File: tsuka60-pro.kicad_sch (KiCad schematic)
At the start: 168 parts, among them J1 USB_C_Receptacle_USB2.0, J2 Conn_01x04_MountingPin, SW1 SW_Reset, U1 ATmega32U4-M, U2 SRV05-4, Y1 16MHz

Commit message: Transferring updates from the Katana60 Pro
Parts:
- J2: footprint Connector_JST:JST_SH_SM04B-SRSS-TB_1x04-1MP_P1.00mm_Horizontal -> Connector_JST:JST_ACH_BM04B-ACHSS-A-GAN-ETF_1x04-1MP_P1.20mm_Vertical
- renumbered MX37-2 to MX37_2, MX39-2 to MX39_2
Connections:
- net 38-2 renamed 37_2
- net 39-2 renamed 39_2
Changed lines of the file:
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@@
     )
   )
-  (global_label "39-2" (shape input) (at 153.67 133.35 180) (fields_autoplaced)
+  (global_label "39_2" (shape input) (at 153.67 133.35 180) (fields_autoplaced)
     (effects (font (size 1.27 1.27)) (justify right))
-    (property "Intersheet References" "${INTERSHEET_REFS}" (id 0) (at 146.0559 133.2706 0)
+    (property "Intersheet References" "${INTERSHEET_REFS}" (id 0) (at 146.6607 133.2706 0)
       (effects (font (size 1.27 1.27)) (justify right) hide)
     )
@@
     )
   )
-  (global_label "38-2" (shape input) (at 128.27 260.35 180) (fields_autoplaced)
+  (global_label "37_2" (shape input) (at 128.27 260.35 180) (fields_autoplaced)
     (effects (font (size 1.27 1.27)) (justify right))
-    (property "Intersheet References" "${INTERSHEET_REFS}" (id 0) (at 120.6559 260.2706 0)
+    (property "Intersheet References" "${INTERSHEET_REFS}" (id 0) (at 121.2607 260.2706 0)
       (effects (font (size 1.27 1.27)) (justify right) hide)
     )
@@
     )
   )
-  (global_label "39-2" (shape input) (at 153.67 260.35 180) (fields_autoplaced)
+  (global_label "39_2" (shape input) (at 153.67 260.35 180) (fields_autoplaced)
     (effects (font (size 1.27 1.27)) (justify right))
-    (property "Intersheet References" "${INTERSHEET_REFS}" (id 0) (at 146.0559 260.2706 0)
+    (property "Intersheet References" "${INTERSHEET_REFS}" (id 0) (at 146.6607 260.2706 0)
       (effects (font (size 1.27 1.27)) (justify right) hide)
     )
@@
     )
   )
-  (global_label "38-2" (shape input) (at 128.27 133.35 180) (fields_autoplaced)
+  (global_label "37_2" (shape input) (at 128.27 133.35 180) (fields_autoplaced)
     (effects (font (size 1.27 1.27)) (justify right))
-    (property "Intersheet References" "${INTERSHEET_REFS}" (id 0) (at 120.6559 133.2706 0)
+    (property "Intersheet References" "${INTERSHEET_REFS}" (id 0) (at 121.2607 133.2706 0)
       (effects (font (size 1.27 1.27)) (justify right) hide)
     )
@@
       (effects (font (size 1.27 1.27)) (justify left))
     )
-    (property "Footprint" "Connector_JST:JST_SH_SM04B-SRSS-TB_1x04-1MP_P1.00mm_Horizontal" (id 2) (at 355.6 201.93 0)
+    (property "Footprint" "Connector_JST:JST_ACH_BM04B-ACHSS-A-GAN-ETF_1x04-1MP_P1.20mm_Vertical" (id 2) (at 355.6 201.93 0)
       (effects (font (size 1.27 1.27)) hide)
     )
@@
   (symbol (lib_id "MX_Alps_Hybrid:MX-NoLED") (at 154.94 256.54 0) (unit 1)
     (in_bom yes) (on_board yes) (fields_autoplaced)
-    (property "Reference" "MX39-2" (id 0) (at 155.8256 250.19 0)
+    (property "Reference" "MX39_2" (id 0) (at 155.8256 250.19 0)
       (effects (font (size 1.524 1.524)))
     )
@@
   (symbol (lib_id "MX_Alps_Hybrid:MX-NoLED") (at 129.54 256.54 0) (unit 1)
     (in_bom yes) (on_board yes) (fields_autoplaced)
-    (property "Reference" "MX37-2" (id 0) (at 130.4256 250.19 0)
+    (property "Reference" "MX37_2" (id 0) (at 130.4256 250.19 0)
       (effects (font (size 1.524 1.524)))
     )
@@
     )
     (path "/08e6d373-2bf3-4f1e-87e0-beb65fb65c5f"
-      (reference "J2") (unit 1) (value "Conn_01x04_MountingPin") (footprint "Connector_JST:JST_SH_SM04B-SRSS-TB_1x04-1MP_P1.00mm_Horizontal")
+      (reference "J2") (unit 1) (value "Conn_01x04_MountingPin") (footprint "Connector_JST:JST_ACH_BM04B-ACHSS-A-GAN-ETF_1x04-1MP_P1.20mm_Vertical")
     )
     (path "/bb3a180f-cdbc-49d0-97a9-6846eb214c84"
@@
     )
     (path "/f5c00a1c-6009-46f7-bb45-59e86d627cba"
-      (reference "MX37-2") (unit 1) (value "MX-NoLED") (footprint "marbastlib-mx:SW_MX_HS_1.25u")
+      (reference "MX37_2") (unit 1) (value "MX-NoLED") (footprint "marbastlib-mx:SW_MX_HS_1.25u")
     )
     (path "/75294b3a-bcf4-4dee-b1b0-009fd10bd357"
@@
     )
     (path "/a8b3e0bc-cfe9-4e81-954e-c1b4323435ec"
-      (reference "MX39-2") (unit 1) (value "MX-NoLED") (footprint "marbastlib-mx:SW_MX_HS_1.25u")
+      (reference "MX39_2") (unit 1) (value "MX-NoLED") (footprint "marbastlib-mx:SW_MX_HS_1.25u")
     )
     (path "/f1689421-be27-441f-a091-cda9d302f953"

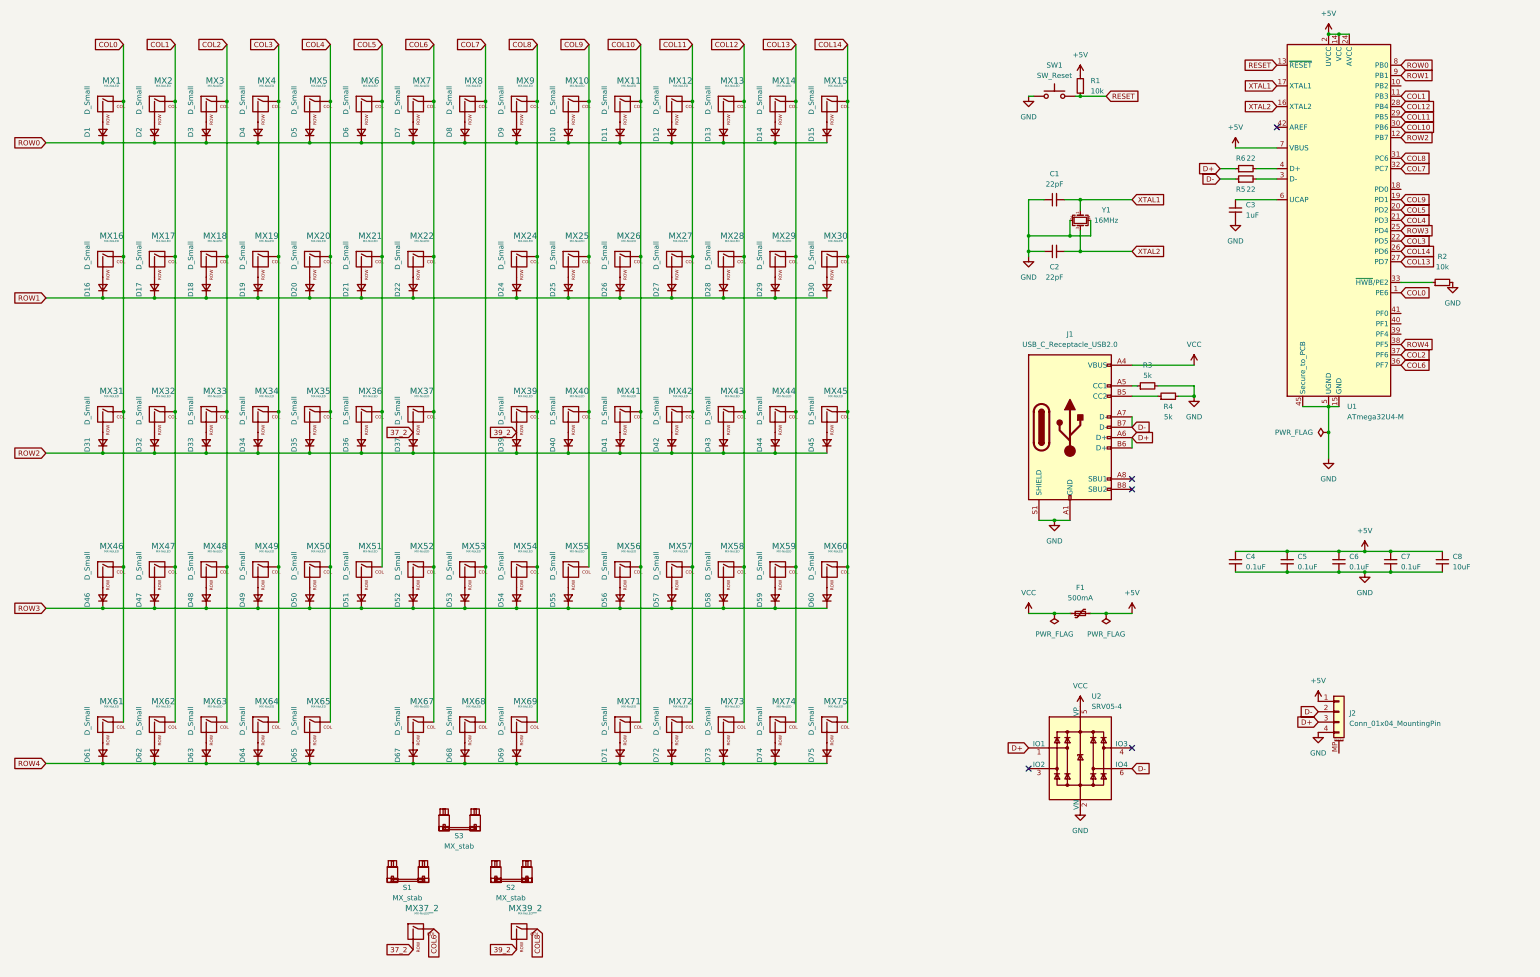
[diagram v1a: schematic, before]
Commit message: Update the schematic, footprints and layout
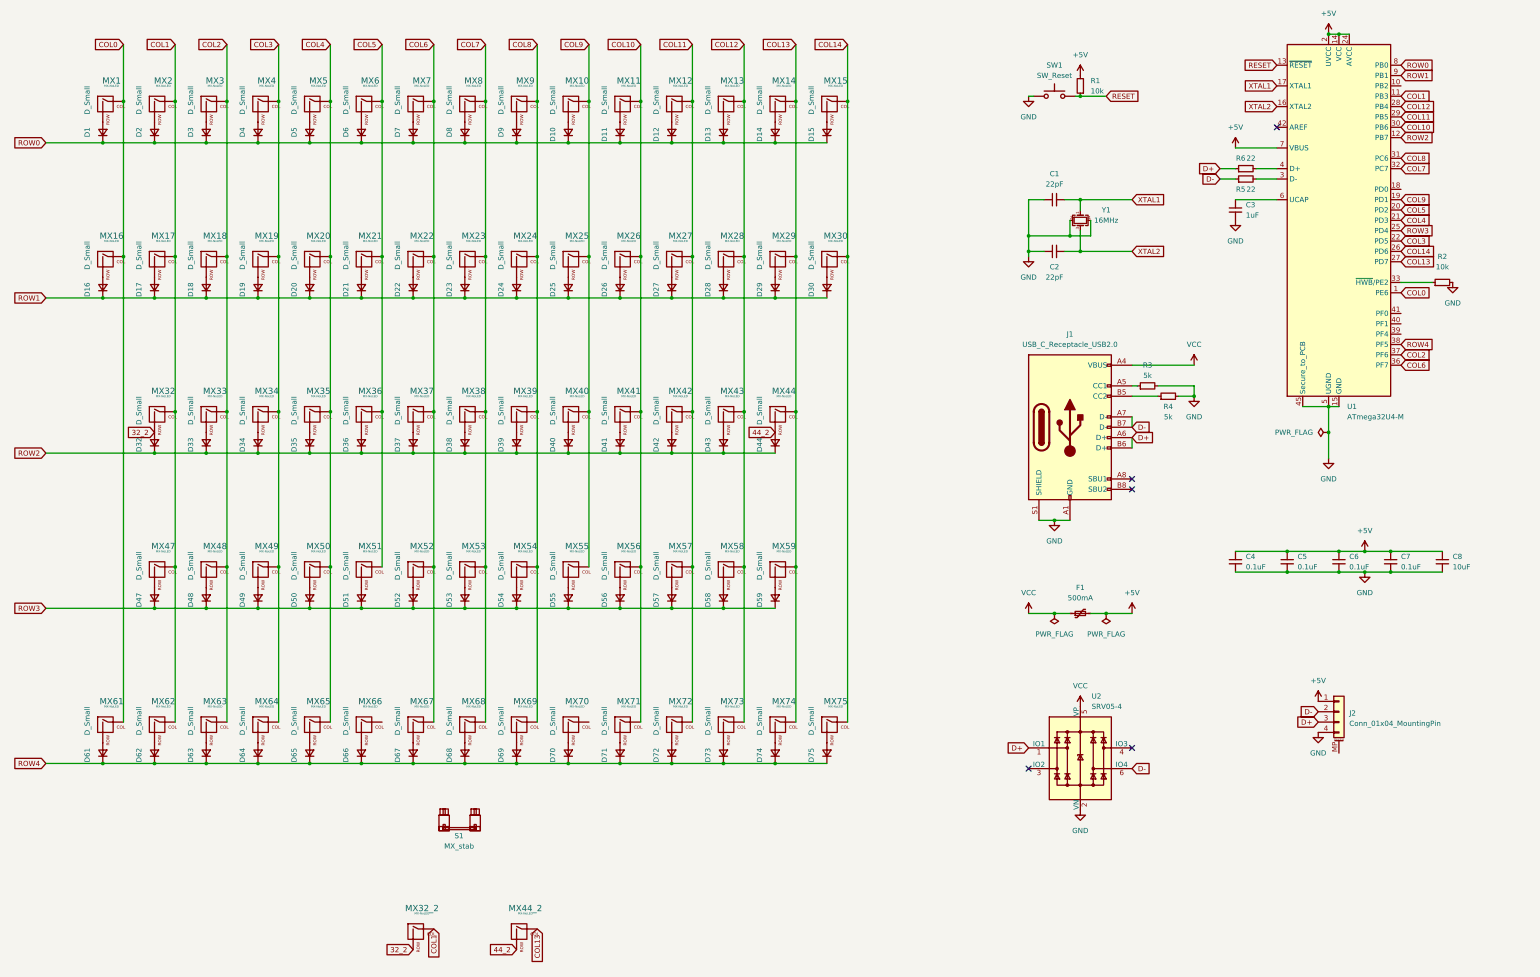
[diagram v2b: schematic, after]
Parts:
- removed D31, D45, D46, D60: D_Small, Diode_SMD:D_SOD-123, symbol Device:D_Small
- removed MX31, MX45: MX-NoLED, marbastlib-mx:SW_MX_HS_1.25u, symbol MX_Alps_Hybrid:MX-NoLED
- removed MX46, MX60: MX-NoLED, marbastlib-mx:SW_MX_HS_1u, symbol MX_Alps_Hybrid:MX-NoLED
- removed S1, S2: MX_stab, marbastlib-mx:STAB_MX_2u, symbol marbastlib-mx:MX_stab
- added D23, D38, D66, D70: D_Small, Diode_SMD:D_SOD-123, symbol Device:D_Small
- added MX23: MX-NoLED, marbastlib-mx:SW_MX_HS_1u, symbol MX_Alps_Hybrid:MX-NoLED
- added MX38: MX-NoLED, marbastlib-mx:SW_MX_HS_1.5u, symbol MX_Alps_Hybrid:MX-NoLED
- added MX66, MX70: MX-NoLED, marbastlib-mx:SW_MX_HS_1.25u, symbol MX_Alps_Hybrid:MX-NoLED
- MX16, MX30: footprint marbastlib-mx:SW_MX_HS_1.5u -> marbastlib-mx:SW_MX_HS_1u
- MX32, MX44: footprint marbastlib-mx:SW_MX_HS_1u -> marbastlib-mx:SW_MX_HS_1.75u
- MX32_2: renamed from MX37_2; footprint marbastlib-mx:SW_MX_HS_1.25u -> marbastlib-mx:SW_MX_HS_1.75u_stp
- MX44_2: renamed from MX39_2; footprint marbastlib-mx:SW_MX_HS_1.25u -> marbastlib-mx:SW_MX_HS_1.75u_stp
- MX47, MX59: footprint marbastlib-mx:SW_MX_HS_1u -> marbastlib-mx:SW_MX_HS_1.5u
- MX65, MX71: footprint marbastlib-mx:SW_MX_HS_1u -> marbastlib-mx:SW_MX_HS_1.25u
- renumbered S3 to S1
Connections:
- net COL1: now also MX32_2.1 (COL)
- net COL13: now also MX44_2.1 (COL)
- net COL6: no longer MX32_2.1 (COL)
- net COL7: now also MX23.1 (COL), MX38.1 (COL)
- net COL8: no longer MX44_2.1 (COL)
- net ROW1: now also D23.1 (K)
- net ROW2: now also D38.1 (K)
- net ROW4: now also D66.1 (K), D70.1 (K)
- net 32_2: now reaches D32.2 (A), MX32.2 (ROW)
- net 32_2: now also MX32_2.2 (ROW)
- net 44_2: now reaches D44.2 (A), MX44.2 (ROW)
- net 44_2: now also MX44_2.2 (ROW)
- net 37_2: no longer names the net of D37.2 (A), MX37.2 (ROW)
- net 37_2: no longer MX32_2.2 (ROW)
- net 39_2: no longer names the net of D39.2 (A), MX39.2 (ROW)
- net 39_2: no longer MX44_2.2 (ROW)
- new net: D70.2 (A), MX70.2 (ROW)
- new net: D23.2 (A), MX23.2 (ROW)
- new net: D66.2 (A), MX66.2 (ROW)
- new net: D38.2 (A), MX38.2 (ROW)

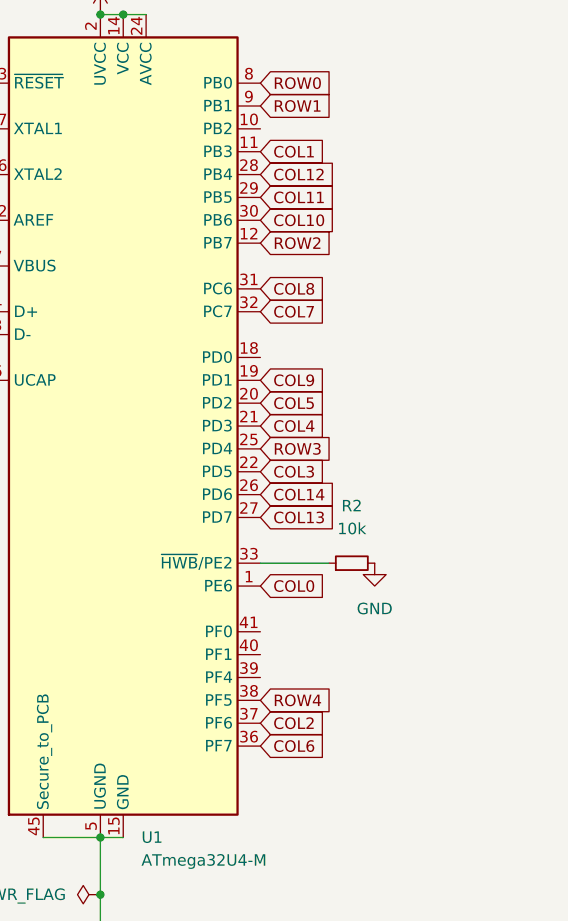
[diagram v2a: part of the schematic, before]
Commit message: Further update traces
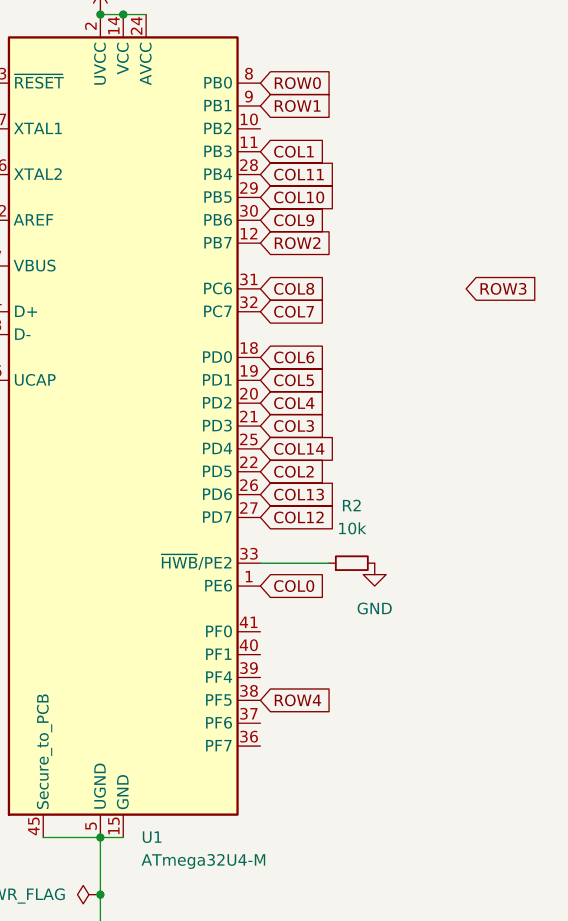
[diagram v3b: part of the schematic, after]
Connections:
- net COL10: now also U1.29 (PB5); no longer U1.30 (PB6)
- net COL11: now also U1.28 (PB4); no longer U1.29 (PB5)
- net COL12: now also U1.27 (PD7); no longer U1.28 (PB4)
- net COL13: now also U1.26 (PD6); no longer U1.27 (PD7)
- net COL14: now also U1.25 (PD4); no longer U1.26 (PD6)
- net COL2: now also U1.22 (PD5); no longer U1.37 (PF6)
- net COL3: now also U1.21 (PD3); no longer U1.22 (PD5)
- net COL4: now also U1.20 (PD2); no longer U1.21 (PD3)
- net COL5: now also U1.19 (PD1); no longer U1.20 (PD2)
- net COL6: now also U1.18 (PD0); no longer U1.36 (PF7)
- net COL9: now also U1.30 (PB6); no longer U1.19 (PD1)
- net ROW3: no longer U1.25 (PD4)

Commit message: Finish traces, draft 1
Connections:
- net COL0: now also U1.40 (PF1); no longer U1.1 (PE6)
- net COL1: now also U1.39 (PF4); no longer U1.11 (PB3)
- net COL2: now also U1.36 (PF7); no longer U1.22 (PD5)
- net COL3: now also U1.22 (PD5); no longer U1.21 (PD3)
- net ROW0: now also U1.12 (PB7); no longer U1.8 (PB0)
- net ROW1: now also U1.41 (PF0); no longer U1.9 (PB1)
- net ROW2: now also U1.21 (PD3); no longer U1.12 (PB7)
- net ROW3: now also U1.37 (PF6)
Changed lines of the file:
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@@
     )
   )
-  (global_label "COL0" (shape input) (at 370.84 99.06 0) (fields_autoplaced)
-    (effects (font (size 1.27 1.27)) (justify left))
-    (property "Intersheet References" "${INTERSHEET_REFS}" (id 0) (at 378.0912 99.1394 0)
-      (effects (font (size 1.27 1.27)) (justify left) hide)
-    )
-  )
-  (global_label "ROW3" (shape input) (at 393.7 66.04 0) (fields_autoplaced)
-    (effects (font (size 1.27 1.27)) (justify left))
-    (property "Intersheet References" "${INTERSHEET_REFS}" (id 0) (at 401.3745 66.1194 0)
+  (global_label "COL0" (shape input) (at 370.84 106.68 0) (fields_autoplaced)
+    (effects (font (size 1.27 1.27)) (justify left))
+    (property "Intersheet References" "${INTERSHEET_REFS}" (id 0) (at 378.0912 106.7594 0)
+      (effects (font (size 1.27 1.27)) (justify left) hide)
+    )
+  )
+  (global_label "ROW3" (shape input) (at 370.84 114.3 0) (fields_autoplaced)
+    (effects (font (size 1.27 1.27)) (justify left))
+    (property "Intersheet References" "${INTERSHEET_REFS}" (id 0) (at 378.5145 114.3794 0)
       (effects (font (size 1.27 1.27)) (justify left) hide)
     )
@@
     )
   )
-  (global_label "COL3" (shape input) (at 370.84 81.28 0) (fields_autoplaced)
-    (effects (font (size 1.27 1.27)) (justify left))
-    (property "Intersheet References" "${INTERSHEET_REFS}" (id 0) (at 378.0912 81.3594 0)
+  (global_label "COL3" (shape input) (at 370.84 86.36 0) (fields_autoplaced)
+    (effects (font (size 1.27 1.27)) (justify left))
+    (property "Intersheet References" "${INTERSHEET_REFS}" (id 0) (at 378.0912 86.4394 0)
       (effects (font (size 1.27 1.27)) (justify left) hide)
     )
@@
     )
   )
-  (global_label "ROW2" (shape input) (at 370.84 60.96 0) (fields_autoplaced)
+  (global_label "ROW2" (shape input) (at 370.84 81.28 0) (fields_autoplaced)
+    (effects (font (size 1.27 1.27)) (justify left))
+    (property "Intersheet References" "${INTERSHEET_REFS}" (id 0) (at 378.5145 81.3594 0)
+      (effects (font (size 1.27 1.27)) (justify left) hide)
+    )
+  )
+  (global_label "D+" (shape input) (at 304.8 134.62 0) (fields_autoplaced)
+    (effects (font (size 1.27 1.27)) (justify left))
+    (property "Intersheet References" "${INTERSHEET_REFS}" (id 0) (at 310.0555 134.5406 0)
+      (effects (font (size 1.27 1.27)) (justify left) hide)
+    )
+  )
+  (global_label "COL13" (shape input) (at 370.84 88.9 0) (fields_autoplaced)
+    (effects (font (size 1.27 1.27)) (justify left))
+    (property "Intersheet References" "${INTERSHEET_REFS}" (id 0) (at 379.3007 88.9794 0)
+      (effects (font (size 1.27 1.27)) (justify left) hide)
+    )
+  )
+  (global_label "ROW4" (shape input) (at 370.84 111.76 0) (fields_autoplaced)
+    (effects (font (size 1.27 1.27)) (justify left))
+    (property "Intersheet References" "${INTERSHEET_REFS}" (id 0) (at 378.5145 111.8394 0)
+      (effects (font (size 1.27 1.27)) (justify left) hide)
+    )
+  )
+  (global_label "COL13" (shape input) (at 158.75 255.27 270) (fields_autoplaced)
+    (effects (font (size 1.27 1.27)) (justify right))
+    (property "Intersheet References" "${INTERSHEET_REFS}" (id 0) (at 158.6706 263.7307 90)
+      (effects (font (size 1.27 1.27)) (justify right) hide)
+    )
+  )
+  (global_label "ROW0" (shape input) (at 370.84 60.96 0) (fields_autoplaced)
     (effects (font (size 1.27 1.27)) (justify left))
     (property "Intersheet References" "${INTERSHEET_REFS}" (id 0) (at 378.5145 61.0394 0)
@@
     )
   )
-  (global_label "D+" (shape input) (at 304.8 134.62 0) (fields_autoplaced)
-    (effects (font (size 1.27 1.27)) (justify left))
-    (property "Intersheet References" "${INTERSHEET_REFS}" (id 0) (at 310.0555 134.5406 0)
-      (effects (font (size 1.27 1.27)) (justify left) hide)
-    )
-  )
-  (global_label "COL13" (shape input) (at 370.84 88.9 0) (fields_autoplaced)
-    (effects (font (size 1.27 1.27)) (justify left))
-    (property "Intersheet References" "${INTERSHEET_REFS}" (id 0) (at 379.3007 88.9794 0)
-      (effects (font (size 1.27 1.27)) (justify left) hide)
-    )
-  )
-  (global_label "ROW4" (shape input) (at 370.84 111.76 0) (fields_autoplaced)
-    (effects (font (size 1.27 1.27)) (justify left))
-    (property "Intersheet References" "${INTERSHEET_REFS}" (id 0) (at 378.5145 111.8394 0)
-      (effects (font (size 1.27 1.27)) (justify left) hide)
-    )
-  )
-  (global_label "COL13" (shape input) (at 158.75 255.27 270) (fields_autoplaced)
-    (effects (font (size 1.27 1.27)) (justify right))
-    (property "Intersheet References" "${INTERSHEET_REFS}" (id 0) (at 158.6706 263.7307 90)
-      (effects (font (size 1.27 1.27)) (justify right) hide)
-    )
-  )
-  (global_label "ROW0" (shape input) (at 370.84 43.18 0) (fields_autoplaced)
-    (effects (font (size 1.27 1.27)) (justify left))
-    (property "Intersheet References" "${INTERSHEET_REFS}" (id 0) (at 378.5145 43.2594 0)
-      (effects (font (size 1.27 1.27)) (justify left) hide)
-    )
-  )
   (global_label "COL2" (shape input) (at 82.55 38.1 180) (fields_autoplaced)
     (effects (font (size 1.27 1.27)) (justify right))
@@
     )
   )
-  (global_label "ROW1" (shape input) (at 370.84 45.72 0) (fields_autoplaced)
-    (effects (font (size 1.27 1.27)) (justify left))
-    (property "Intersheet References" "${INTERSHEET_REFS}" (id 0) (at 378.5145 45.7994 0)
+  (global_label "ROW1" (shape input) (at 370.84 104.14 0) (fields_autoplaced)
+    (effects (font (size 1.27 1.27)) (justify left))
+    (property "Intersheet References" "${INTERSHEET_REFS}" (id 0) (at 378.5145 104.2194 0)
       (effects (font (size 1.27 1.27)) (justify left) hide)
     )
@@
     )
   )
-  (global_label "COL2" (shape input) (at 370.84 86.36 0) (fields_autoplaced)
-    (effects (font (size 1.27 1.27)) (justify left))
-    (property "Intersheet References" "${INTERSHEET_REFS}" (id 0) (at 378.0912 86.4394 0)
+  (global_label "COL2" (shape input) (at 370.84 116.84 0) (fields_autoplaced)
+    (effects (font (size 1.27 1.27)) (justify left))
+    (property "Intersheet References" "${INTERSHEET_REFS}" (id 0) (at 378.0912 116.9194 0)
       (effects (font (size 1.27 1.27)) (justify left) hide)
     )
@@
     )
   )
-  (global_label "COL1" (shape input) (at 370.84 50.8 0) (fields_autoplaced)
-    (effects (font (size 1.27 1.27)) (justify left))
-    (property "Intersheet References" "${INTERSHEET_REFS}" (id 0) (at 378.0912 50.8794 0)
-      (effects (font (size 1.27 1.27)) (justify left) hide)
-    )
+  (global_label "COL1" (shape input) (at 370.84 109.22 0) (fields_autoplaced)
+    (effects (font (size 1.27 1.27)) (justify left))
+    (property "Intersheet References" "${INTERSHEET_REFS}" (id 0) (at 378.0912 109.2994 0)
+      (effects (font (size 1.27 1.27)) (justify left) hide)
+    )
